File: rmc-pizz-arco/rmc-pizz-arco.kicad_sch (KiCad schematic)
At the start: 80 parts, among them J1 PZT, J2 PZT, J3 PZT, J4 PZT, J5 PZT, J6 PZT, J7 DIN-8, J8 PIZZ/ARCO, U1 OPA4191, U2 OPA4191, U3 OPA4191, U4 CD4066B, U5 CD4066B

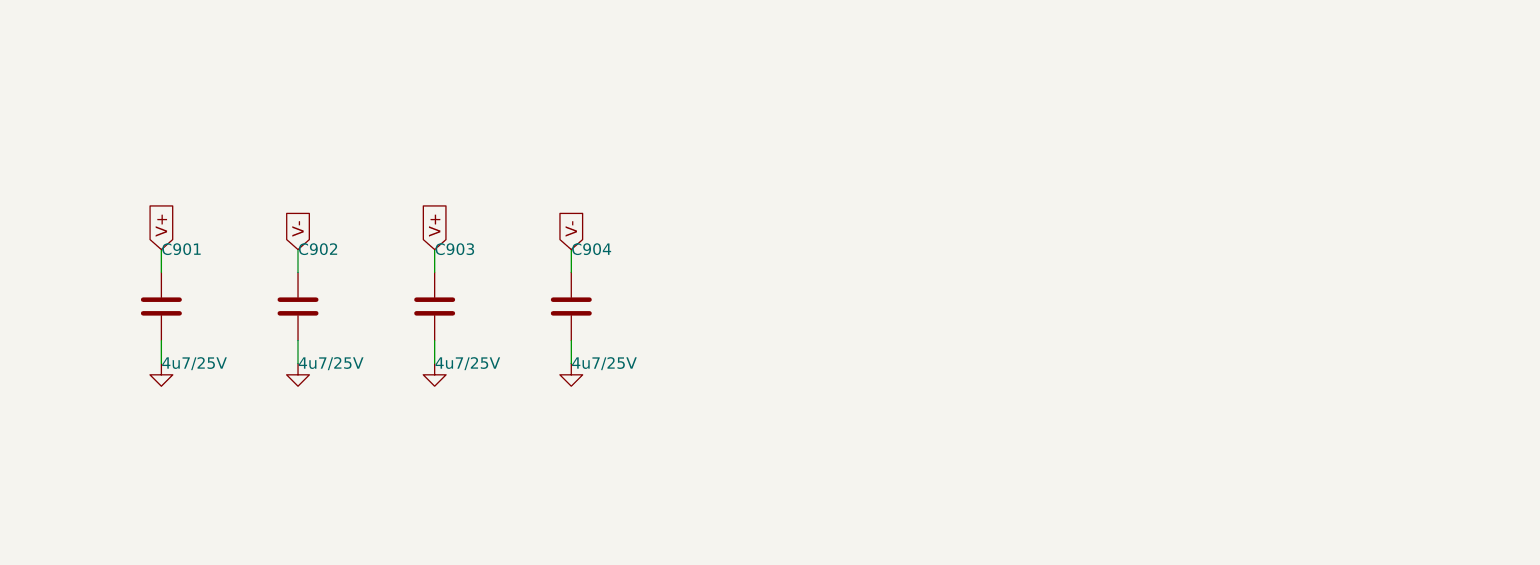
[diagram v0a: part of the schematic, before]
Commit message: Implemented latest round of recommendations from RMC
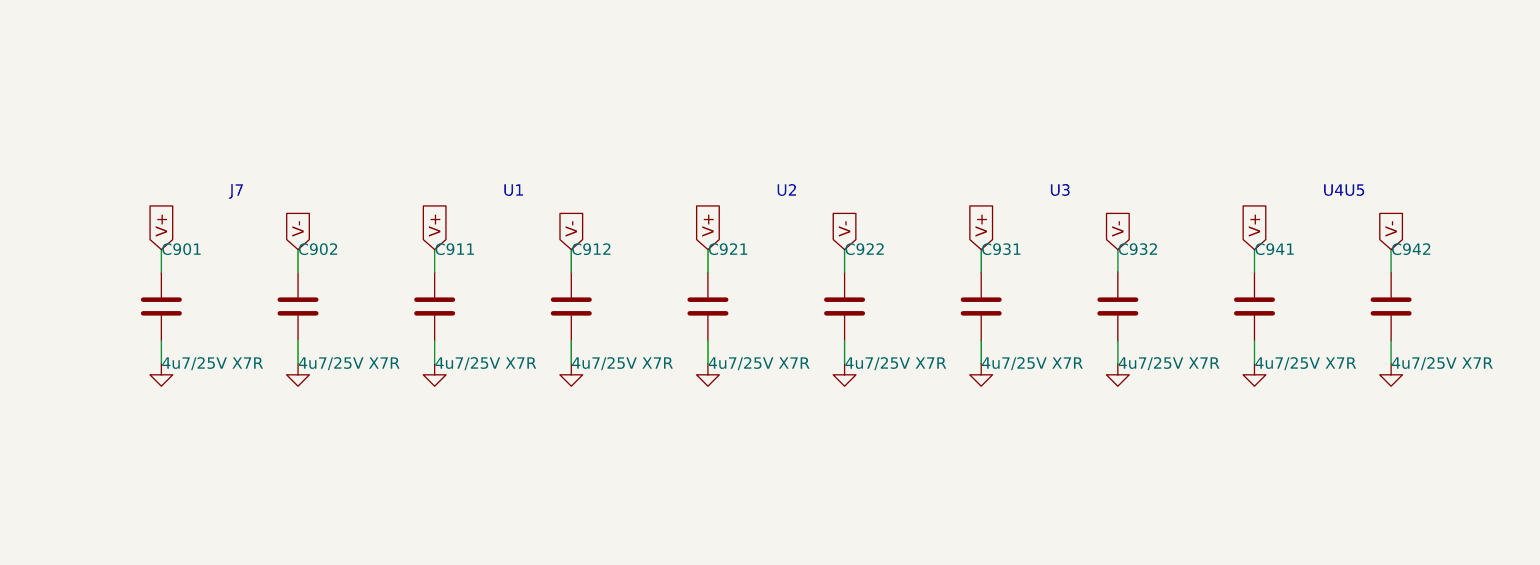
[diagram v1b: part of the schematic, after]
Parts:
- removed C903, C904: 4u7/25V, Capacitor_SMD:C_1206_3216Metric, symbol Device:C
- added C911, C912, C921, C922, C931, C932, C941, C942: 4u7/25V X7R, Capacitor_SMD:C_1206_3216Metric, symbol Device:C
- C901, C902: value 4u7/25V -> 4u7/25V X7R
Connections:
- net AGND: now also C911.2, C912.2, C921.2, C922.2, C931.2, C932.2, C941.2, C942.2
- net V+: now also C911.1, C921.1, C931.1, C941.1
- net V-: now also C912.1, C922.1, C932.1, C942.1
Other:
- note added: "J7"
- note added: "U1"
- note added: "U2"
- note added: "U3"
- note added: "U4U5"

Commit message: Implemented latest round of recommendations from RMC
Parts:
- removed R103, R203, R303, R403, R503, R603: 1k, Resistor_SMD:R_1206_3216Metric, symbol Device:R
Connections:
- net at R604.1, R605.1, U3.7: now also U3.6 (-)
- net at R304.1, R305.1, U2.1: now also U2.2 (-)
- net at R204.1, R205.1, U1.7: now also U1.6 (-)
- net at U2.6 (-): now also R404.1, R405.1, U2.7
- net at U3.2 (-): now also R504.1, R505.1, U3.1
- net at R104.1, R105.1, U1.1: now also U1.2 (-)
